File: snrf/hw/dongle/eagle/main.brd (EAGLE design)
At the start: 100 x 80 mm, 12 parts, among them IC1 FT232RL, U1 ADP3338AKCZ-2.5RL7

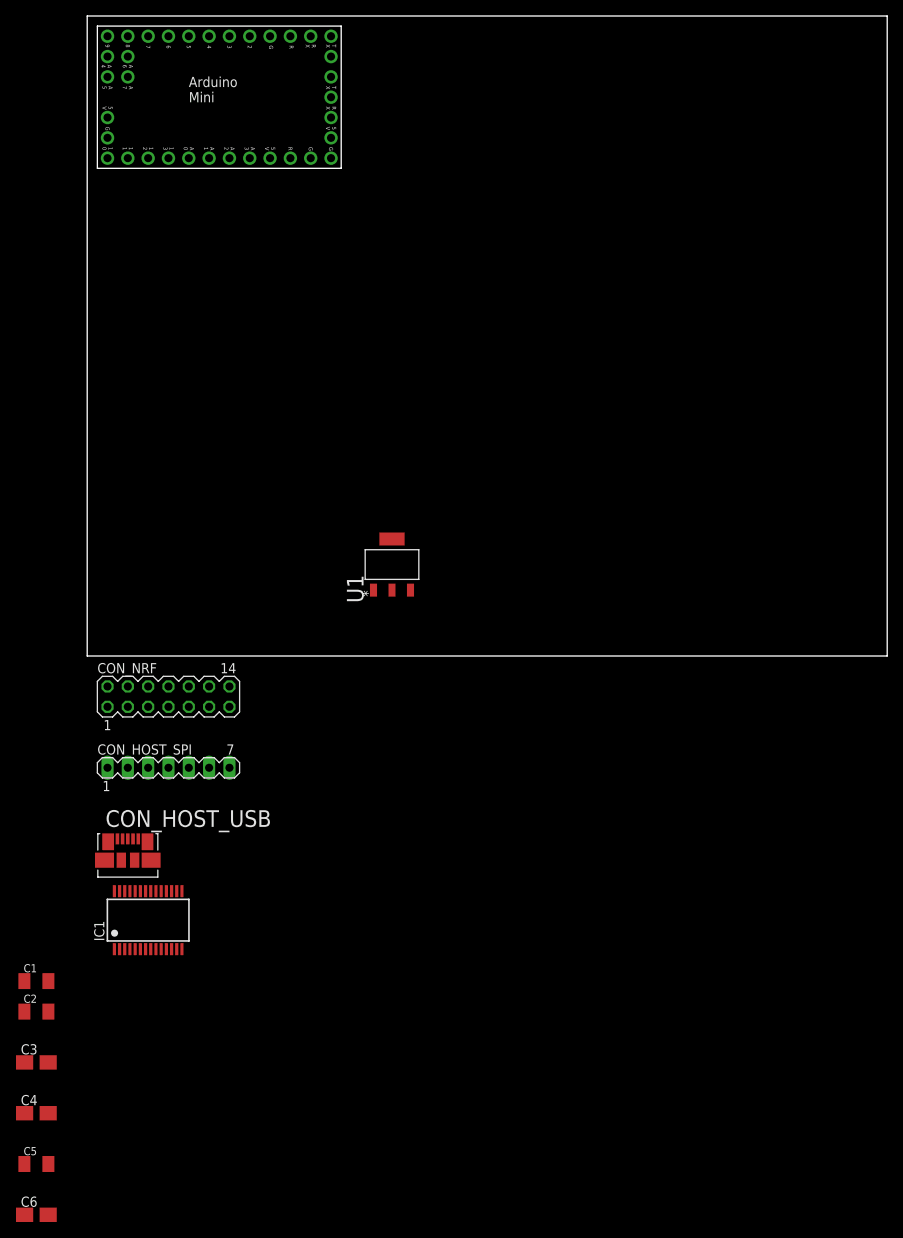
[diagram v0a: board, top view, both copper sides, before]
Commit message: [ update ] schematics done, board routed. nrf connector has to be moved for fitting
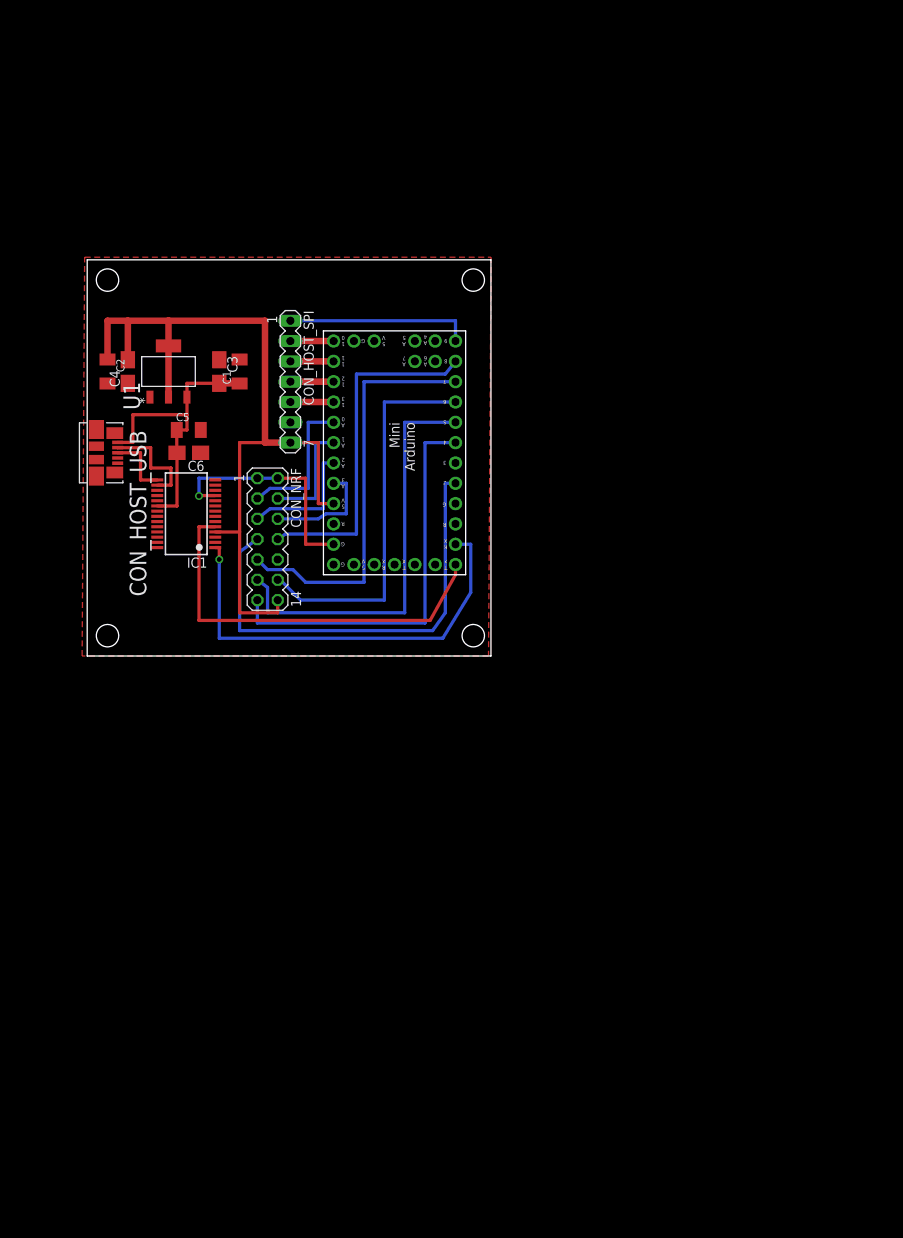
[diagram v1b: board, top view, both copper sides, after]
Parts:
- moved C6 97.1 mm to (12.7, 25.4), turned to 180 degrees
- moved C5 93.7 mm to (12.7, 28.3)
- moved C4 93.4 mm to (5.08, 35.6), turned to 90 degrees
- moved C3 89.3 mm to (16.5, 35.6), turned to 270 degrees
- moved C2 80.5 mm to (2.54, 35.6), turned to 270 degrees
- moved C1 80.3 mm to (19.1, 35.6), turned to 90 degrees
- moved IC1 51.0 mm to (12.4, 17.8), turned to 90 degrees
- moved CON_HOST_SPI 50.6 mm to (25.4, 34.3), turned to 270 degrees
- moved CON_HOST_USB 48.3 mm to (3.81, 25.4), turned to 270 degrees
- moved U1 36.9 mm to (10.2, 35.6)
- moved PCB1 34.8 mm to (29.5, 40.6), turned to 270 degrees
- moved CON_NRF 23.3 mm to (22.5, 14.6), turned to 270 degrees
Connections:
- net NRF_AM: now also PCB1.8; no longer PCB1.5
- net NRF_CD: now also PCB1.7; no longer PCB1.8
- net NRF_PWR: now also PCB1.5; no longer PCB1.7
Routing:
- net HOST_VCC_3V3: track 0.00 -> 104.2 mm
- net NRF_DR: track 0.00 -> 56.9 mm
- net MCU_RXI: track 0.00 -> 54.4 mm, vias 0 -> 1
- net NRF_PWR: track 0.00 -> 52.1 mm
- net NRF_CD: track 0.00 -> 51.0 mm
- net MCU_TXO: track 0.00 -> 50.4 mm
- net NRF_TXEN: track 0.00 -> 50.2 mm
- net NRF_CE: track 0.00 -> 48.0 mm
- net NRF_AM: track 0.00 -> 43.2 mm
- net HOST_VCC_5V: track 0.00 -> 37.8 mm
- net GND: track 0.00 -> 29.4 mm, vias 0 -> 1
- net HOST_IRQ: track 0.00 -> 23.2 mm
- net NRF_CSN: track 0.00 -> 18.2 mm
- net NRF_MOSI: track 0.00 -> 15.7 mm
- net NRF_MISO: track 0.00 -> 14.2 mm
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- added copper zone on layer 1, net GND
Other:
- board size 100 x 80 mm -> 50.5 x 49.5 mm

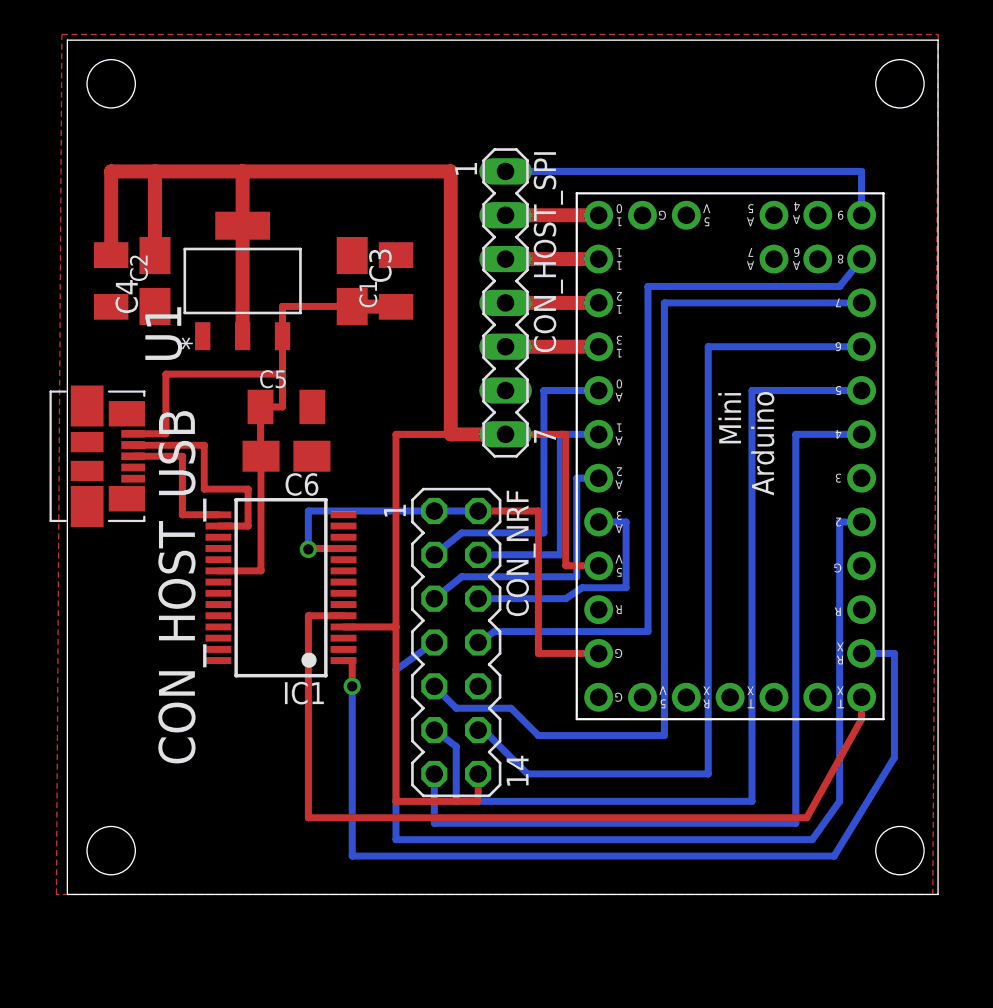
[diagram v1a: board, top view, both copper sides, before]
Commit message: [ update ] rerouted to fit nrf board
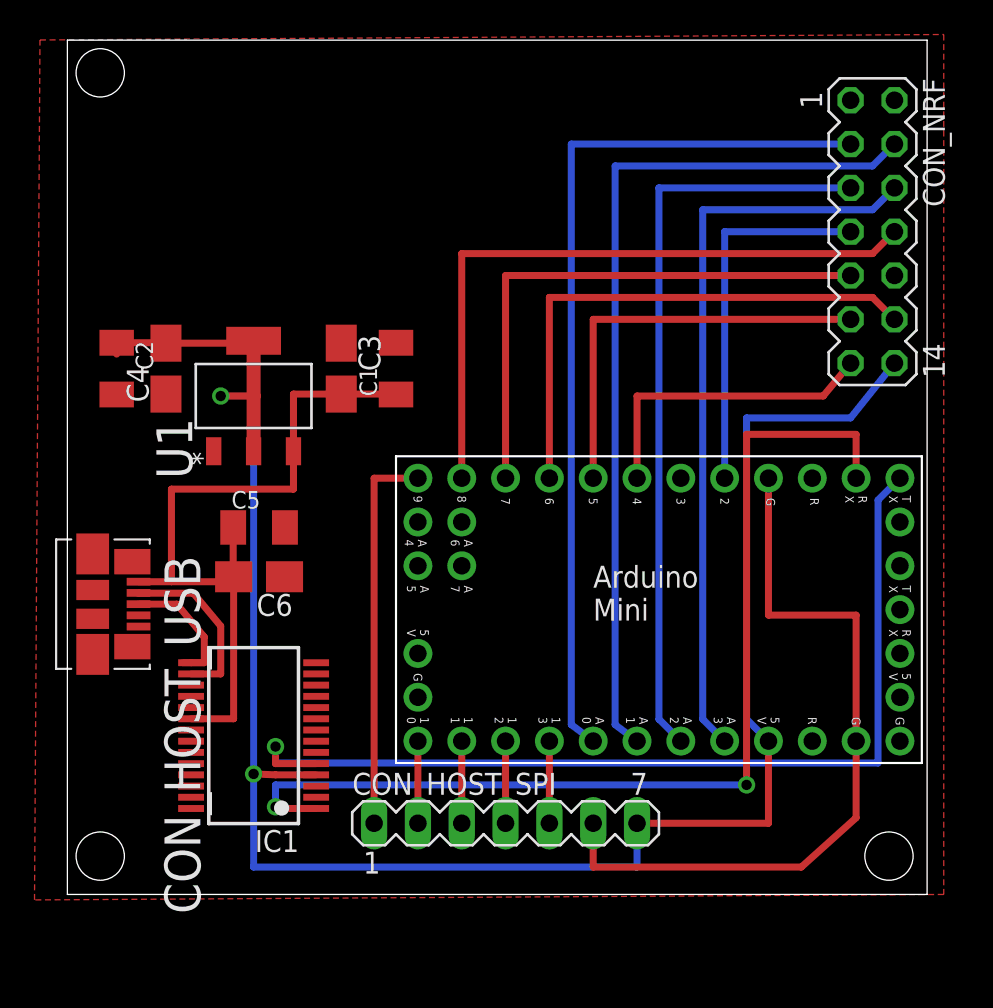
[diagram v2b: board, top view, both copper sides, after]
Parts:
- moved PCB1 34.6 mm to (19.1, 7.62), turned to 0 degrees
- moved CON_NRF 33.9 mm to (46.7, 38.4)
- moved CON_HOST_SPI 30.2 mm to (25.4, 4.13), turned to 0 degrees
- moved IC1 8.72 mm to (10.8, 9.21)
- moved CON_HOST_USB 8.58 mm to (4.13, 16.8)
- moved C5 7.16 mm to (11.1, 21.3)
- moved C6 7.16 mm to (11.1, 18.4)
- moved U1 6.70 mm to (10.8, 28.9)
- moved C3 5.12 mm to (15.9, 30.5)
- moved C4 5.12 mm to (5.71, 30.5)
- moved C2 5.09 mm to (2.86, 30.5)
- moved C1 5.08 mm to (19.1, 30.5)
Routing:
- net NRF_SCK: track 14.0 -> 50.7 mm
- net NRF_DR: track 56.9 -> 21.6 mm
- net NRF_CSN: track 18.2 -> 51.4 mm
- net NRF_TXEN: track 50.2 -> 18.0 mm
- net NRF_MISO: track 14.2 -> 43.0 mm
- net NRF_MOSI: track 15.7 -> 43.7 mm
- net NRF_PWR: track 52.1 -> 24.1 mm
- net NRF_CD: track 51.0 -> 31.8 mm
- net NRF_CE: track 48.0 -> 31.0 mm
- net GND: track 29.4 -> 43.6 mm, vias 1 -> 0
- net HOST_VCC_3V3: track 104.2 -> 116.3 mm, vias 0 -> 2
- net HOST_VCC_5V: track 37.8 -> 43.9 mm
- net MCU_TXO: track 50.4 -> 56.3 mm, vias 0 -> 1
- net MCU_RXI: track 54.4 -> 60.2 mm, vias 1 -> 2
- net NRF_AM: track 43.2 -> 38.6 mm
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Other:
- board size 50.5 x 49.5 mm -> 49.8 x 49.5 mm

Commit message: [ update ] clean tNames
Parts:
- U1: value ADP3338AKCZ-2.5RL7 -> LDO33
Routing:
- net GND: track 43.6 -> 58.2 mm
- net HOST_VCC_5V: track 43.9 -> 37.2 mm
- net MCU_RXI: track 60.2 -> 58.9 mm
